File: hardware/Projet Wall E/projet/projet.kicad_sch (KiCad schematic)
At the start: 0 parts

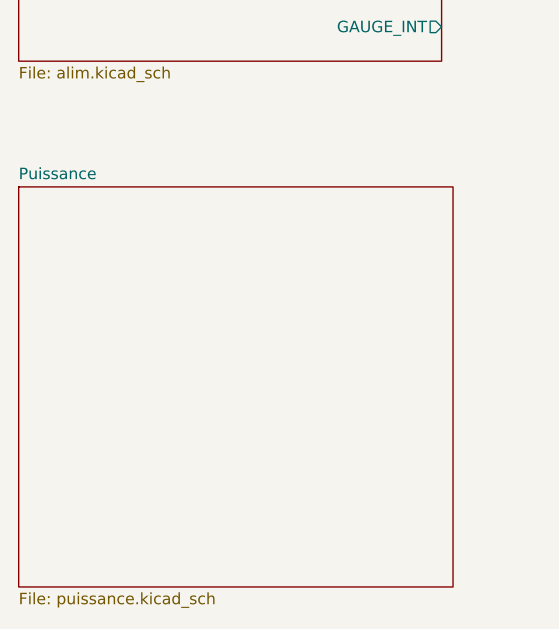
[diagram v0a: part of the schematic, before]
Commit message: feat(moteur): renommage puissance en moteur et modif schéma
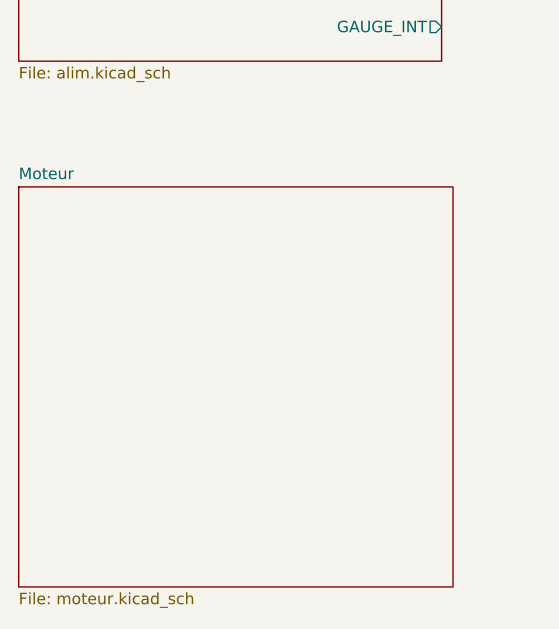
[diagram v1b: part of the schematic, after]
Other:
- sheet Puissance renamed Moteur
- sheet Moteur: file puissance.kicad_sch -> moteur.kicad_sch
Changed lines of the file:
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@@
 			(color 0 0 0 0)
 		)
-		(property "Sheetname" "Puissance"
+		(property "Sheetname" "Moteur"
 			(at 53.34 102.1584 0)
 			(show_name no)
@@
 			)
 		)
-		(property "Sheetfile" "puissance.kicad_sch"
+		(property "Sheetfile" "moteur.kicad_sch"
 			(at 53.34 147.9046 0)
 			(show_name no)

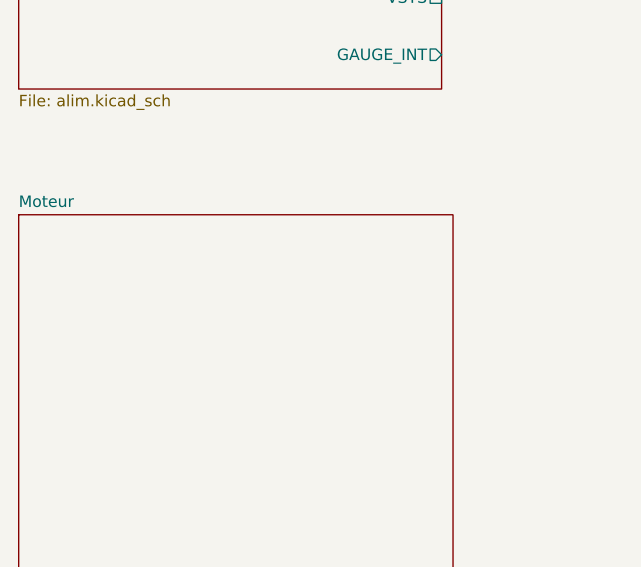
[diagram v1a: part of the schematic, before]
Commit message: fix(moteur): ajustements du schema moteur
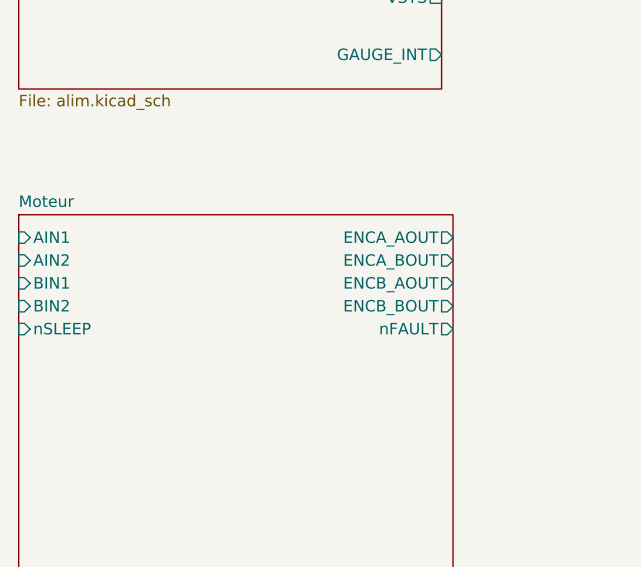
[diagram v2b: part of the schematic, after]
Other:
- sheet Moteur ports: added AIN1, AIN2, BIN1, BIN2, ENCA_AOUT, ENCA_BOUT, ENCB_AOUT, ENCB_BOUT, nFAULT, nSLEEP; removed none
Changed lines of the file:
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@@
+			)
+		)
+		(pin "AIN1" input
+			(at 53.34 105.41 180)
+			(effects
+				(font
+					(size 1.27 1.27)
+				)
+				(justify left)
+			)
+		)
+		(pin "AIN2" input
+			(at 53.34 107.95 180)
+			(effects
+				(font
+					(size 1.27 1.27)
+				)
+				(justify left)
+			)
+		)
+		(pin "BIN1" input
+			(at 53.34 110.49 180)
+			(effects
+				(font
+					(size 1.27 1.27)
+				)
+				(justify left)
+			)
+		)
+		(pin "BIN2" input
+			(at 53.34 113.03 180)
+			(effects
+				(font
+					(size 1.27 1.27)
+				)
+				(justify left)
+			)
+		)
+		(pin "nSLEEP" input
+			(at 53.34 115.57 180)
+			(effects
+				(font
+					(size 1.27 1.27)
+				)
+				(justify left)
+			)
+		)
+		(pin "ENCA_AOUT" output
+			(at 101.6 105.41 0)
+			(effects
+				(font
+					(size 1.27 1.27)
+				)
+				(justify right)
+			)
+		)
+		(pin "ENCA_BOUT" output
+			(at 101.6 107.95 0)
+			(effects
+				(font
+					(size 1.27 1.27)
+				)
+				(justify right)
+			)
+		)
+		(pin "ENCB_AOUT" output
+			(at 101.6 110.49 0)
+			(effects
+				(font
+					(size 1.27 1.27)
+				)
+				(justify right)
+			)
+		)
+		(pin "ENCB_BOUT" output
+			(at 101.6 113.03 0)
+			(effects
+				(font
+					(size 1.27 1.27)
+				)
+				(justify right)
+			)
+		)
+		(pin "nFAULT" output
+			(at 101.6 115.57 0)
+			(effects
+				(font
+					(size 1.27 1.27)
+				)
+				(justify right)
 			)
 		)
